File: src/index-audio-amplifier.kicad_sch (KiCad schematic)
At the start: 60 parts, among them J1 USB_B_Micro, Q1 DMG1012T, SW1 SW_Push, U1 RP2040, U2 RT6150B-33GQW, U3 W25Q16JVUXIQ, U4 PCM5101A, U5 TLV70033_SOT23-5, X1 12MHz

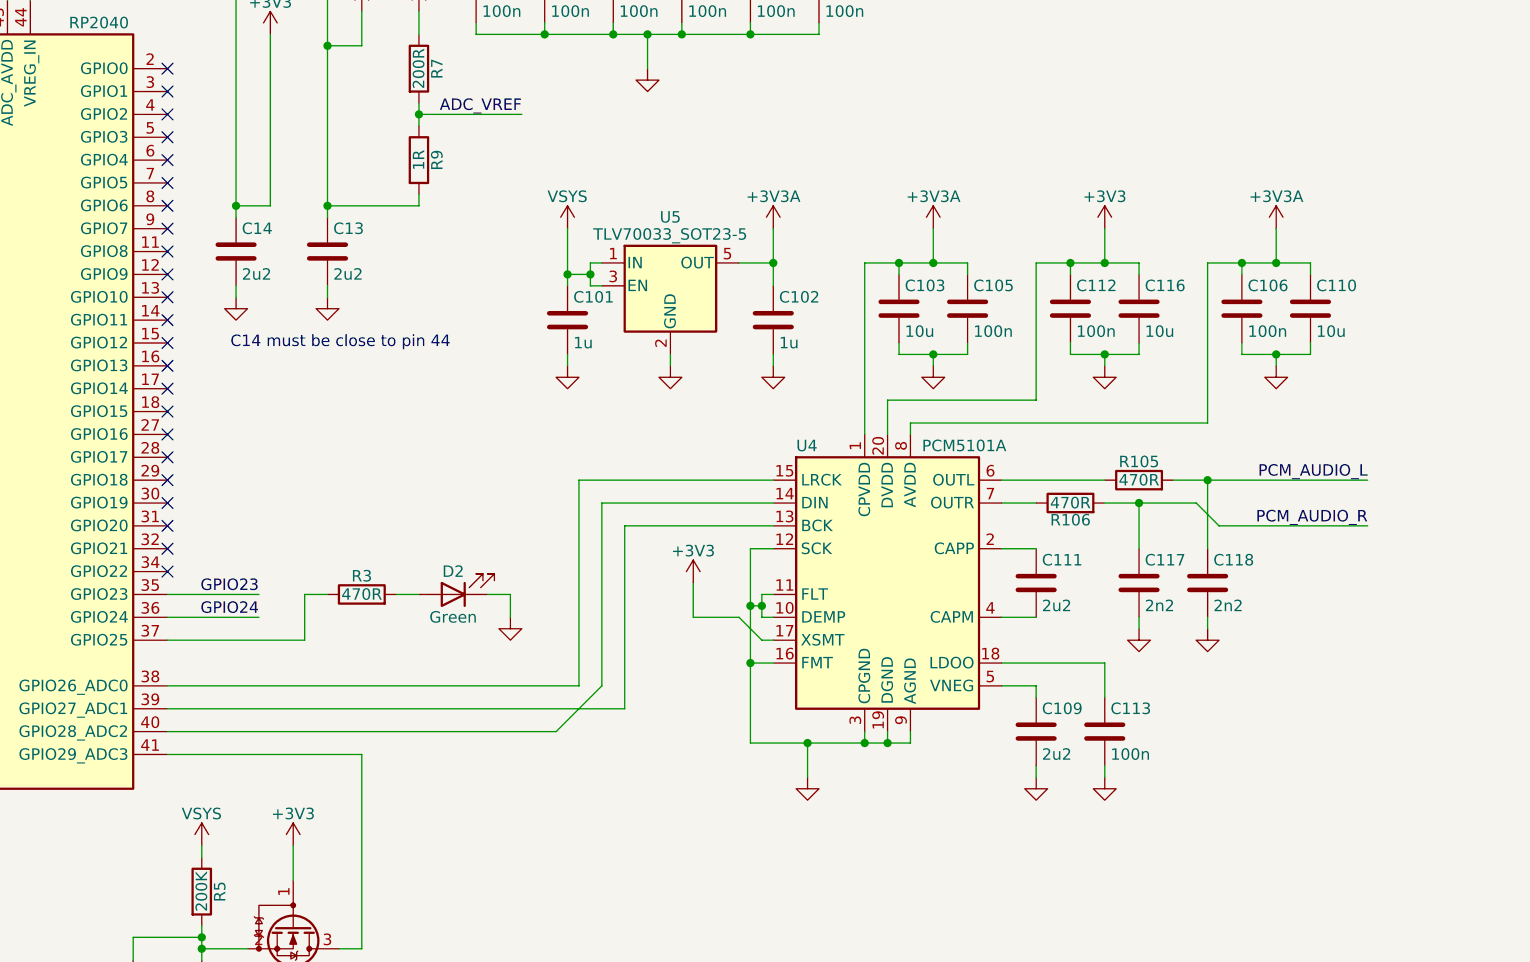
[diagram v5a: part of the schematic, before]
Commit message: Move I2S pins to match `picoamp` firmware
Refererenced firmware is on the branch `picoamp-rebase` in the
index-audio-interface repository:
<https://gitlab.com/recursivenomad/index-audio-interface/-/tree/picoamp-rebase/>

Which itself is rebased from sctanf's picoamp `main` branch:
<https://github.com/sctanf/picoamp/>
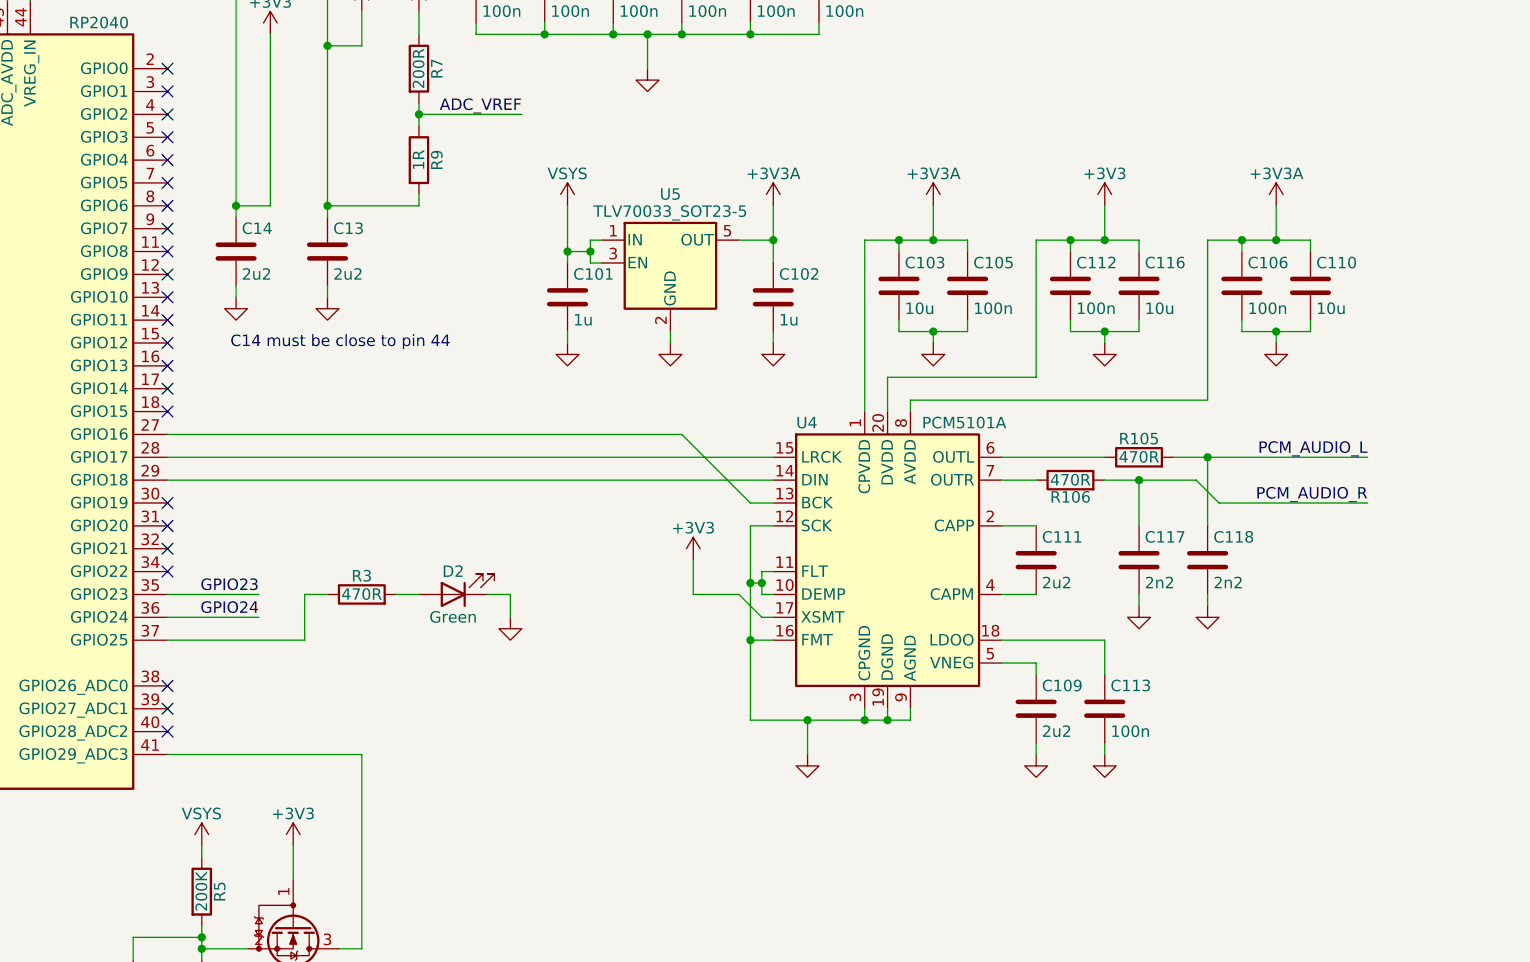
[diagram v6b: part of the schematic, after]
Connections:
- net at U4.13 (BCK): now also U1.27 (GPIO16); no longer U1.39 (GPIO27_ADC1)
- net at U4.14 (DIN): now also U1.29 (GPIO18); no longer U1.40 (GPIO28_ADC2)
- net at U4.15 (LRCK): now also U1.28 (GPIO17); no longer U1.38 (GPIO26_ADC0)
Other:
- moved on the sheet: C101, C102, C103, C105, C106, C109, C110, C111, C112, C113, C116, C117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

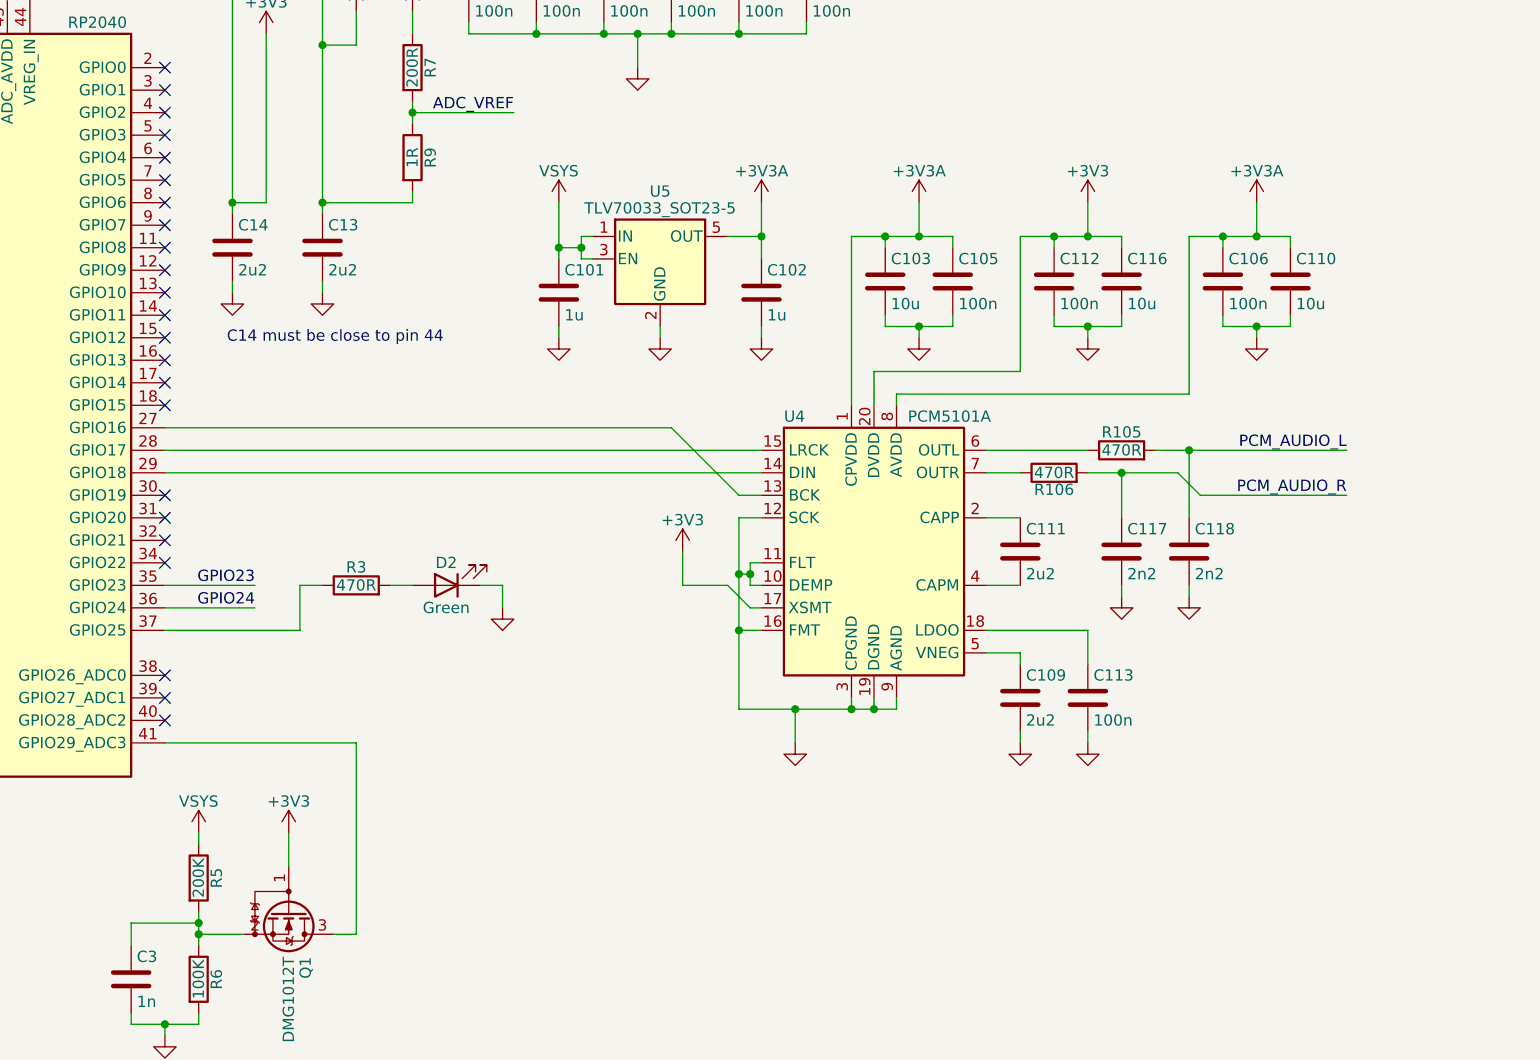
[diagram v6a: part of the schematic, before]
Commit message: Replace PCM5101A with 2 MAX98360CENL
Should be functionally matched to the picoamp firmware now.

Schematic follows stereo "Typical Application Circuit" from MAX98360x
datasheet:
<https://www.analog.com/media/en/technical-documentation/data-sheets/max98360a-max98360d.pdf>
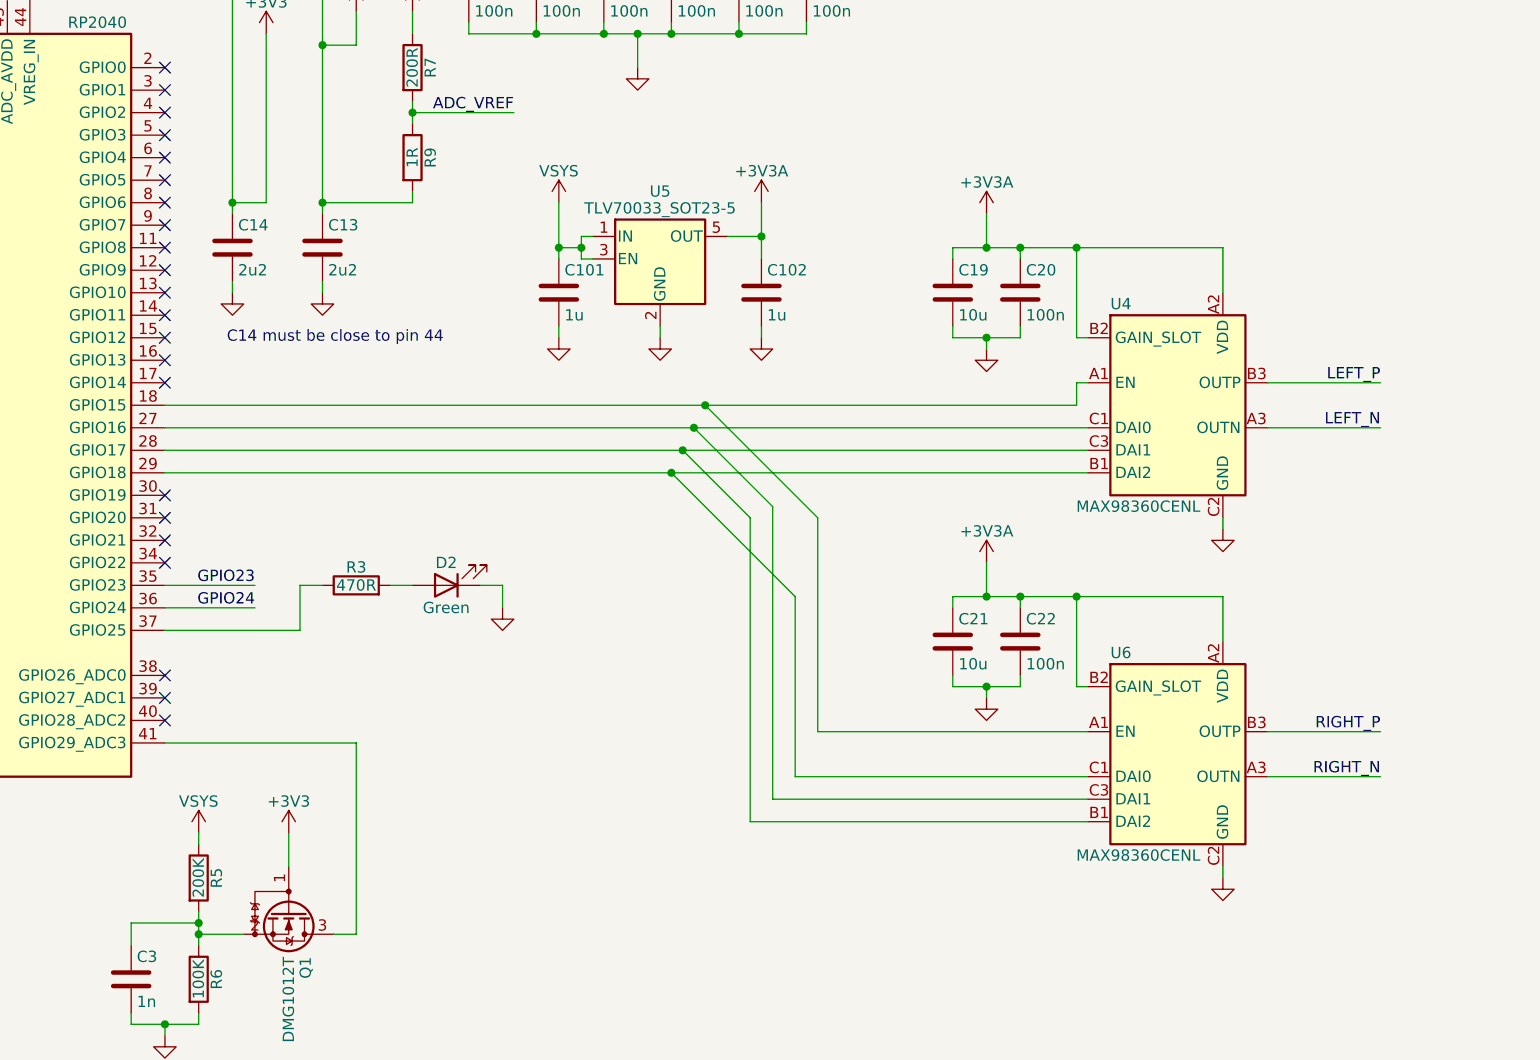
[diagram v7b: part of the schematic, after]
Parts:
- removed C103, C110, C116: 10u, Capacitor_SMD:C_01005_0402Metric, symbol Device:C
- removed C105, C106, C112, C113: 100n, Capacitor_SMD:C_01005_0402Metric, symbol Device:C
- removed C109, C111: 2u2, Capacitor_SMD:C_01005_0402Metric, symbol Device:C
- removed C117, C118: 2n2, Capacitor_SMD:C_01005_0402Metric, symbol Device:C
- removed R105, R106: 470R, Resistor_SMD:R_0402_1005Metric, symbol Device:R
- removed U4: PCM5101A, Package_SO:TSSOP-20_4.4x6.5mm_P0.65mm, symbol Audio:PCM5101A
- added C19, C21: 10u, Capacitor_SMD:C_01005_0402Metric, symbol Device:C
- added C20, C22: 100n, Capacitor_SMD:C_01005_0402Metric, symbol Device:C
- added U4, U6: MAX98360CENL, Package_BGA:WLP-9_1.468x1.448mm_Layout3x3_P0.4mm, symbol ProjectSymbols_IndexAudioAmplifier:MAX98360xENL
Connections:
- net +3V3A: now also C19.1, C20.1, C21.1, C22.1, U4.A2 (VDD), U4.B2 (GAIN_SLOT), U6.A2 (VDD), U6.B2 (GAIN_SLOT)
- net GND: now also C19.2, C20.2, C21.2, C22.2, U4.C2 (GND), U6.C2 (GND)
- net at U1.27 (GPIO16): now also U4.C1 (DAI0), U6.C3 (DAI1)
- net at U1.29 (GPIO18): now also U4.B1 (DAI2), U6.C1 (DAI0)
- net at U1.28 (GPIO17): now also U4.C3 (DAI1), U6.B1 (DAI2)
- net at U1.18 (GPIO15): now also U4.A1 (EN), U6.A1 (EN)
- new net LEFT_N: U4.A3 (OUTN)
- new net LEFT_P: U4.B3 (OUTP)
- new net RIGHT_N: U6.A3 (OUTN)
- new net RIGHT_P: U6.B3 (OUTP)
- no-connect marks 25 -> 24

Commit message: Remove DNP resistors
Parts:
- removed R15, R4: NO-FIT, Resistor_SMD:R_0402_1005Metric, symbol Device:R
